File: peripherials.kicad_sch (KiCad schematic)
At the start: 58 parts, among them J801 Socket_Samtec_ERF5_2x20_ERF5-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, J802 JST_SH_1x4_SM04B-SRSS-TB-LF-SN, J803 JST_SH_1x4_SM04B-SRSS-TB-LF-SN, J804 JST_SH_1x2_SM02B-SRSS-TB-LF-SN, U801 PN7160AHN, Y801 Resonator_27.12MHz_XRCGB

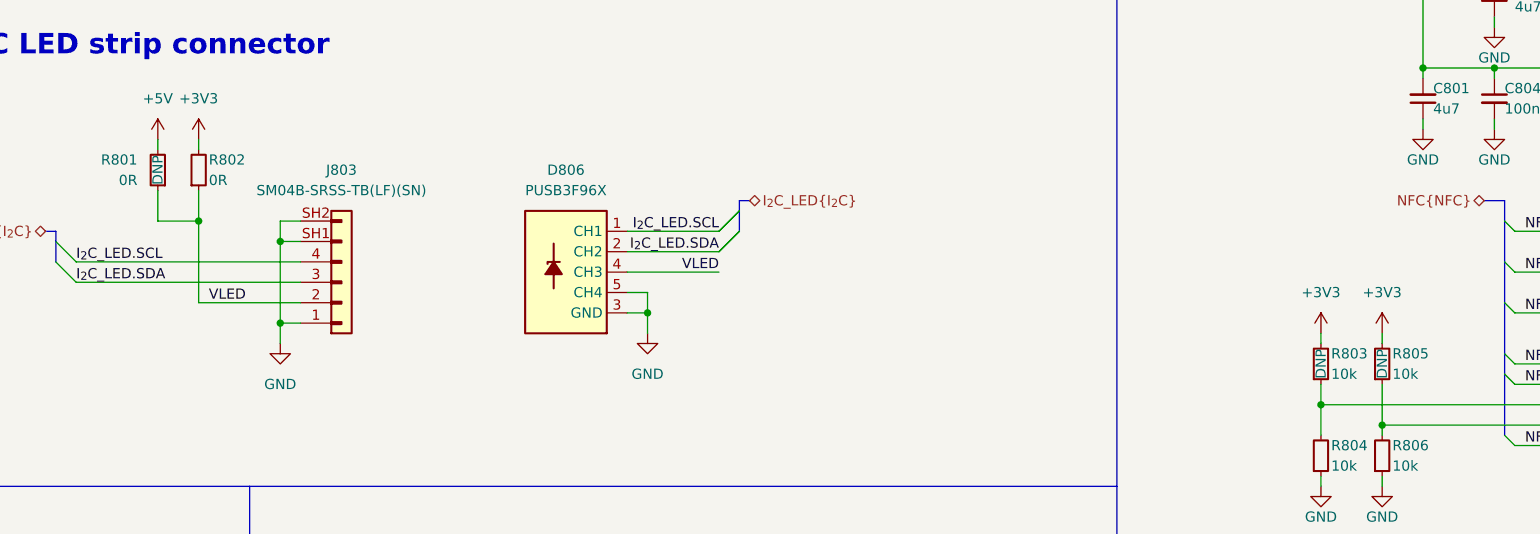
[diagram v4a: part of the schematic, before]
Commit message: Sch: Clean incorrect symbol references; Cleanup DNPs
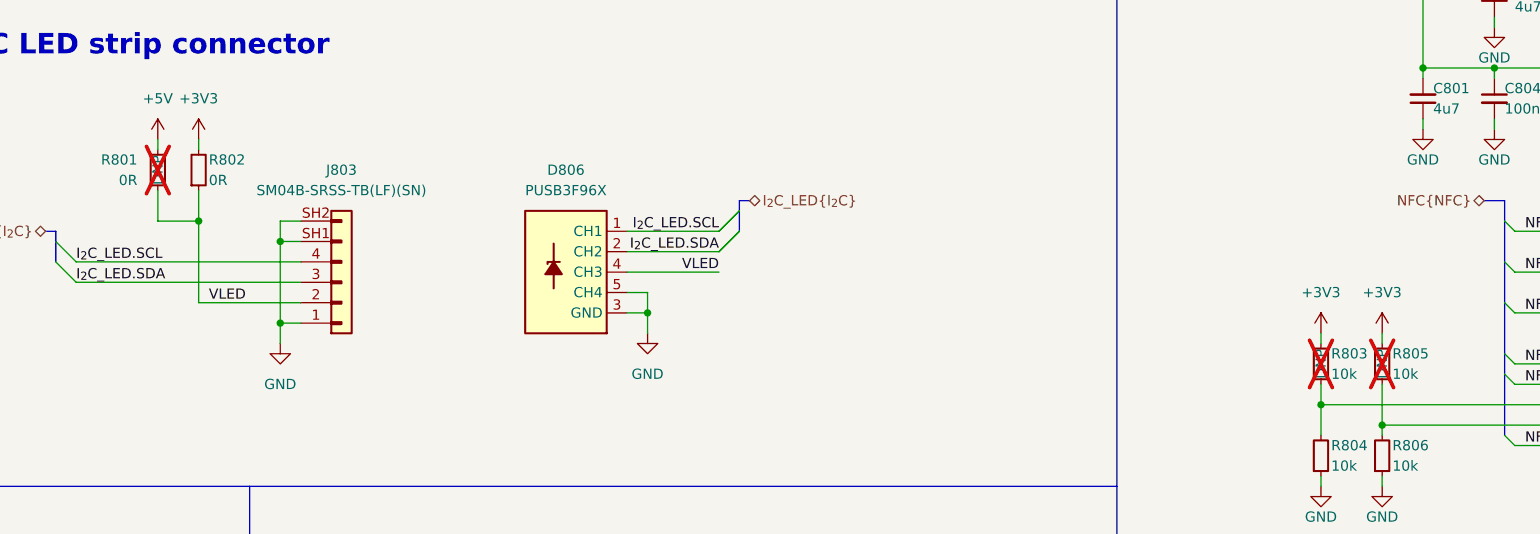
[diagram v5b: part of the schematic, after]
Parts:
- C811, C812, C813, C814, C816, C817, C818, C819, C820, C821, C822, C823, C824, C825, C826, C827, R807, R808, R809, R810: DNP DNP -> (none)
- R801, R803, R805: now not fitted; now left out of the parts list
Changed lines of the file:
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@@
       (effects (font (size 1.27 1.27)) (justify left bottom) hide)
     )
-    (property "DNP" "DNP" (at 369.57 123.19 0)
-      (effects (font (size 1.27 1.27)) hide)
-    )
     (pin "1")
     (pin "2")
@@
       (effects (font (size 1.27 1.27)) (justify left bottom) hide)
     )
-    (property "DNP" "DNP" (at 344.17 100.33 0)
-      (effects (font (size 1.27 1.27)) hide)
-    )
     (pin "1")
     (pin "2")
@@
       (effects (font (size 1.27 1.27)) (justify left bottom) hide)
     )
-    (property "DNP" "DNP" (at 344.17 107.95 0)
-      (effects (font (size 1.27 1.27)) hide)
-    )
     (pin "1")
     (pin "2")
@@
   )
   (symbol (lib_id "antmicroResistors0402:R_10k_0402") (at 236.22 120.65 90) (unit 1)
-    (in_bom yes) (on_board yes) (dnp no)
+    (in_bom no) (on_board yes) (dnp yes)
     (property "Reference" "R803" (at 237.49 116.84 90)
       (effects (font (size 1.27 1.27) (thickness 0.15)) (justify right))
@@
       (effects (font (size 1.27 1.27)) (justify left bottom) hide)
     )
-    (property "DNP" "DNP" (at 322.58 121.92 0)
-      (effects (font (size 1.27 1.27)) hide)
-    )
     (pin "1")
     (pin "2")
@@
       (effects (font (size 1.27 1.27)) (justify left bottom) hide)
     )
-    (property "DNP" "DNP" (at 344.17 130.81 0)
-      (effects (font (size 1.27 1.27)) hide)
-    )
     (pin "1")
     (pin "2")
@@
       (effects (font (size 1.27 1.27)) (justify left bottom) hide)
     )
-    (property "DNP" "DNP" (at 331.47 106.68 0)
-      (effects (font (size 1.27 1.27)) hide)
-    )
     (pin "1")
     (pin "2")
@@
       (effects (font (size 1.27 1.27)) (justify left bottom) hide)
     )
-    (property "DNP" "DNP" (at 331.47 114.3 0)
-      (effects (font (size 1.27 1.27)) hide)
-    )
     (pin "1")
     (pin "2")
@@
   )
   (symbol (lib_id "antmicroResistors0402:R_0R_0402") (at 91.44 96.52 270) (mirror x) (unit 1)
-    (in_bom yes) (on_board yes) (dnp no)
+    (in_bom no) (on_board yes) (dnp yes)
     (property "Reference" "R801" (at 88.9 92.71 90)
       (effects (font (size 1.27 1.27) (thickness 0.15)) (justify right))
@@
       (effects (font (size 1.27 1.27) (thickness 0.15)) (justify left bottom) hide)
     )
-    (property "DNP" "DNP" (at 91.44 93.98 0) (do_not_autoplace)
+    (property "DNP" "DNP" (at 91.44 93.98 0)
       (effects (font (size 1.27 1.27)))
     )
@@
       (effects (font (size 1.27 1.27)) (justify left bottom) hide)
     )
-    (property "DNP" "DNP" (at 314.96 92.71 0)
-      (effects (font (size 1.27 1.27)) hide)
-    )
     (pin "1")
     (pin "2")
@@
       (effects (font (size 1.27 1.27)) (justify left bottom) hide)
     )
-    (property "DNP" "DNP" (at 331.47 121.92 0)
-      (effects (font (size 1.27 1.27)) hide)
-    )
     (pin "1")
     (pin "2")
@@
       (effects (font (size 1.27 1.27)) (justify left bottom) hide)
     )
-    (property "DNP" "DNP" (at 360.68 121.92 0)
-      (effects (font (size 1.27 1.27)) hide)
-    )
     (pin "1")
     (pin "2")
@@
   )
   (symbol (lib_id "antmicroResistors0402:R_10k_0402") (at 243.84 120.65 90) (unit 1)
-    (in_bom yes) (on_board yes) (dnp no)
+    (in_bom no) (on_board yes) (dnp yes)
     (property "Reference" "R805" (at 245.11 116.84 90)
       (effects (font (size 1.27 1.27) (thickness 0.15)) (justify right))
@@
       (effects (font (size 1.27 1.27)) (justify left bottom) hide)
     )
-    (property "DNP" "DNP" (at 369.57 107.95 0)
-      (effects (font (size 1.27 1.27)) hide)
-    )
     (pin "1")
     (pin "2")
@@
       (effects (font (size 1.27 1.27)) (justify left bottom) hide)
     )
-    (property "DNP" "DNP" (at 314.96 138.43 0)
-      (effects (font (size 1.27 1.27)) hide)
-    )
     (pin "1")
     (pin "2")
@@
       (effects (font (size 1.27 1.27)) (justify left bottom) hide)
     )
-    (property "DNP" "DNP" (at 351.79 121.92 0)
-      (effects (font (size 1.27 1.27)) hide)
-    )
     (pin "1")
     (pin "2")
@@
       (effects (font (size 1.27 1.27)) (justify left bottom) hide)
     )
-    (property "DNP" "DNP" (at 314.96 130.81 0)
-      (effects (font (size 1.27 1.27)) hide)
-    )
     (pin "1")
     (pin "2")
@@
       (effects (font (size 1.27 1.27)) (justify left bottom) hide)
     )
-    (property "DNP" "DNP" (at 331.47 124.46 0)
-      (effects (font (size 1.27 1.27)) hide)
-    )
     (pin "1")
     (pin "2")
@@
       (effects (font (size 1.27 1.27)) (justify left bottom) hide)
     )
-    (property "DNP" "DNP" (at 360.68 114.3 0)
-      (effects (font (size 1.27 1.27)) hide)
-    )
     (pin "1")
     (pin "2")
@@
       (effects (font (size 1.27 1.27)) (justify left bottom) hide)
     )
-    (property "DNP" "DNP" (at 344.17 123.19 0)
-      (effects (font (size 1.27 1.27)) hide)
-    )
     (pin "1")
     (pin "2")
@@
       (effects (font (size 1.27 1.27)) (justify left bottom) hide)
     )
-    (property "DNP" "DNP" (at 314.96 100.33 0)
-      (effects (font (size 1.27 1.27)) hide)
-    )
     (pin "1")
     (pin "2")
@@
       (effects (font (size 1.27 1.27)) (justify left bottom) hide)
     )
-    (property "DNP" "DNP" (at 351.79 114.3 0)
-      (effects (font (size 1.27 1.27)) hide)
-    )
     (pin "1")
     (pin "2")
@@
       (effects (font (size 1.27 1.27)) (justify left bottom) hide)
     )
-    (property "DNP" "DNP" (at 322.58 114.3 0)
-      (effects (font (size 1.27 1.27)) hide)
-    )
     (pin "1")

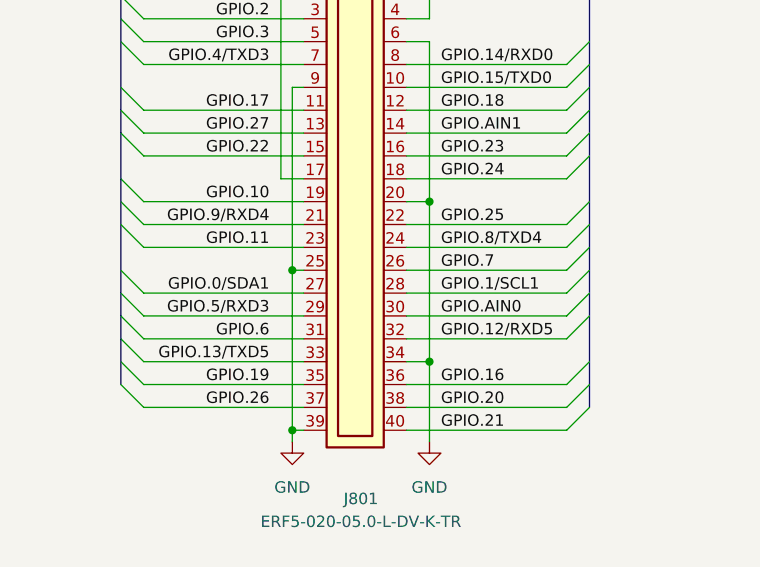
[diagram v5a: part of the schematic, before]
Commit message: Update I2C connections (use GPIO44/45 for board I2C; drop level shifter)
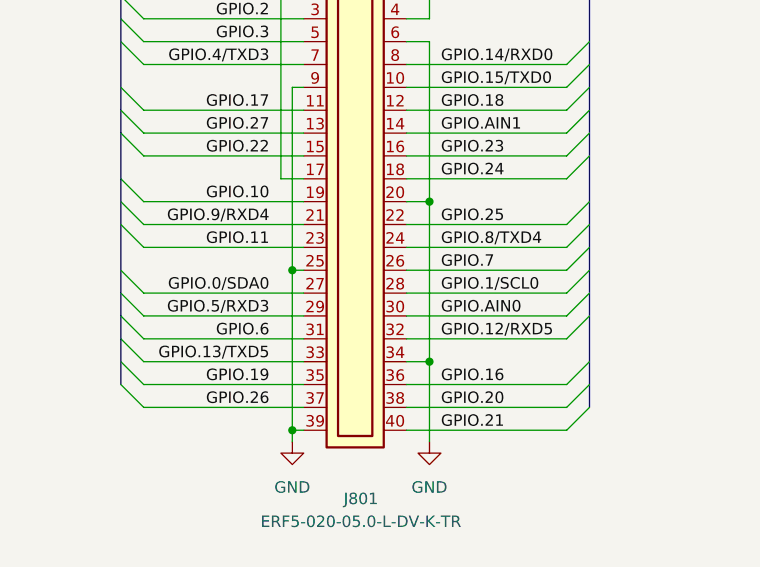
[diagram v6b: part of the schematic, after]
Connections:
- net GPIO.0/SDA1: no longer J801.27
- net GPIO.1/SCL1: no longer J801.28
- new net GPIO.0/SDA0: J801.27
- new net GPIO.1/SCL0: J801.28
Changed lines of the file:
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@@
     (effects (font (size 1.27 1.27)) (justify left bottom))
   )
-  (label "GPIO.0/SDA1" (at 40.64 212.09 180) (fields_autoplaced)
+  (label "GPIO.0{slash}SDA0" (at 40.64 212.09 180) (fields_autoplaced)
     (effects (font (size 1.27 1.27)) (justify right bottom))
   )
@@
     (effects (font (size 1.27 1.27)) (justify left bottom))
   )
-  (label "GPIO.1/SCL1" (at 59.69 212.09 0) (fields_autoplaced)
+  (label "GPIO.1{slash}SCL0" (at 59.69 212.09 0) (fields_autoplaced)
     (effects (font (size 1.27 1.27)) (justify left bottom))
   )

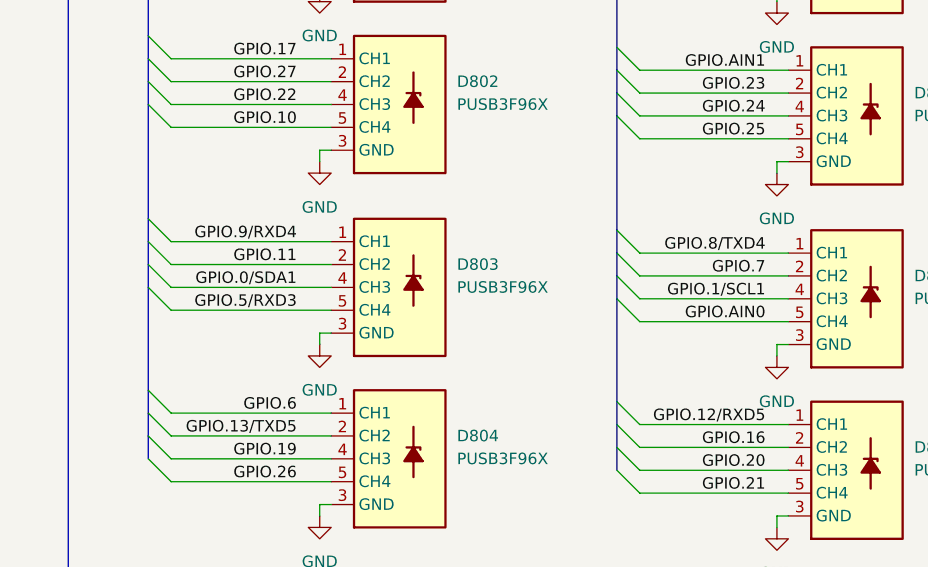
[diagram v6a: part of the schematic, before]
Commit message: [#55181] PCB: Connect GPIOs of CM
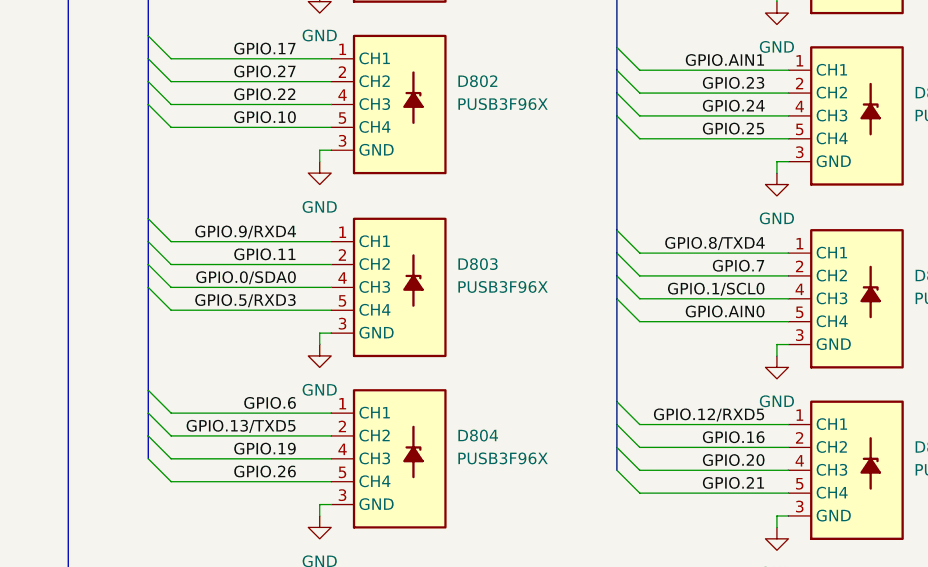
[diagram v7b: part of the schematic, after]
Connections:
- net GPIO.0/SDA1 is gone; now on net GPIO.0/SDA0: D803.4 (CH3), D803.7 (CH3)
- net GPIO.1/SCL1 is gone; now on net GPIO.1/SCL0: D809.4 (CH3), D809.7 (CH3)
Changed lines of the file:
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@@
     (effects (font (size 1.27 1.27)) (justify left bottom))
   )
-  (label "GPIO.0/SDA1" (at 128.27 210.82 180) (fields_autoplaced)
+  (label "GPIO.0{slash}SDA0" (at 128.27 210.82 180) (fields_autoplaced)
     (effects (font (size 1.27 1.27)) (justify right bottom))
   )
@@
     (effects (font (size 1.27 1.27)) (justify left bottom))
   )
-  (label "GPIO.1/SCL1" (at 180.34 212.09 180) (fields_autoplaced)
+  (label "GPIO.1{slash}SCL0" (at 180.34 212.09 180) (fields_autoplaced)
     (effects (font (size 1.27 1.27)) (justify right bottom))
   )

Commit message: [#55532] Sch: Optimize conections for easier routing
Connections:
- net I_{2}C_Sensor.SCL is gone; now on net I_{2}C1.SCL: D805.1 (CH1), D805.10 (CH1), J802.4
- net I_{2}C_Sensor.SDA is gone; now on net I_{2}C1.SDA: D805.2 (CH2), D805.9 (CH2), J802.3
- net NFC.I_{2}C_SCL is gone; now on net I_{2}C1.SCL: U801.7 (I2C_SCL)
- net NFC.I_{2}C_SDA is gone; now on net I_{2}C1.SDA: U801.5 (I2C_SDA)
- net I_{2}C_LED.SCL renamed I_{2}C1.SCL
- net I_{2}C_LED.SDA renamed I_{2}C1.SDA
